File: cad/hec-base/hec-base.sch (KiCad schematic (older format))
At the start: 0 parts

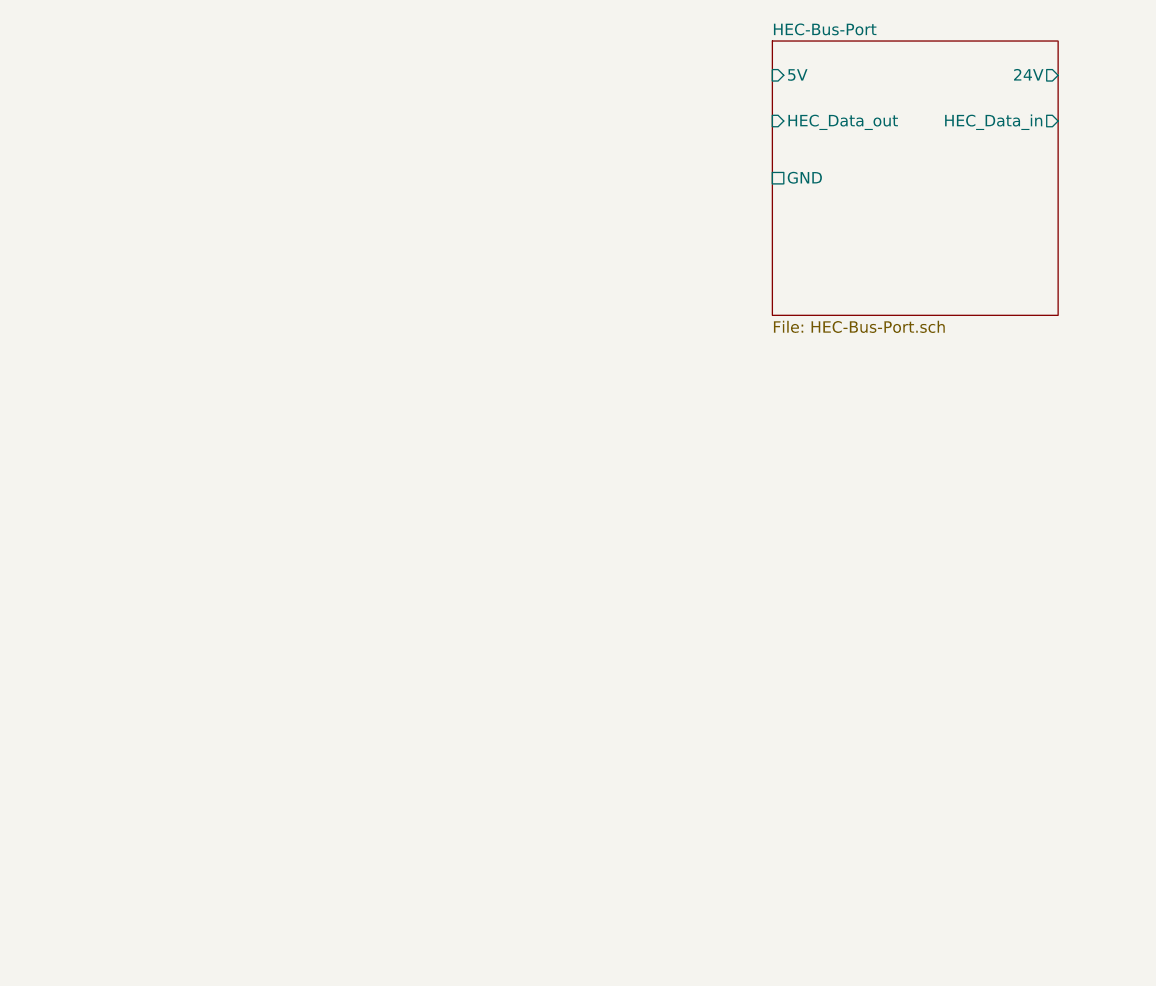
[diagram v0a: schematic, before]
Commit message: Power-Management schematics input and dimensioning done.
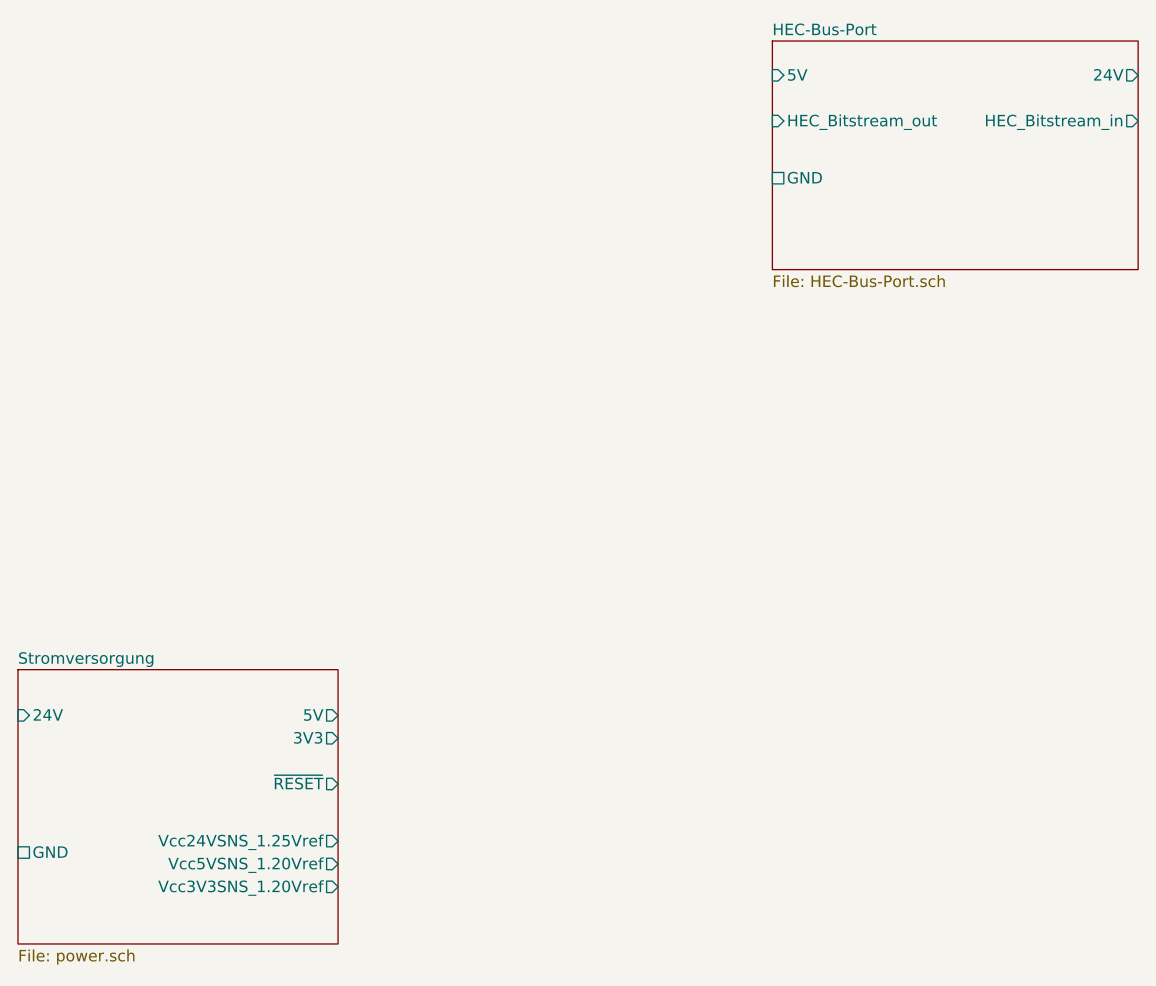
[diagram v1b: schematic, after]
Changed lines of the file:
@@
 $Descr A3 16535 11693
 encoding utf-8
-Sheet 1 2
+Sheet 1 3
 Title "Marienkäfer HEC-Basis-Bord"
 Date "2020-12-28"
@@
 $EndDescr
 $Sheet
-S 11850 1100 1250 1200
+S 8550 3850 1400 1200
+U 6012F6F5
+F0 "Stromversorgung" 50
+F1 "power.sch" 50
+F2 "24V" I L 8550 4050 50
+F3 "GND" U L 8550 4650 50
+F4 "5V" O R 9950 4050 50
+F5 "3V3" O R 9950 4150 50
+F6 "~RESET~" O R 9950 4350 50
+F7 "Vcc24VSNS_1.25Vref" O R 9950 4600 50
+F8 "Vcc5VSNS_1.20Vref" O R 9950 4700 50
+F9 "Vcc3V3SNS_1.20Vref" O R 9950 4800 50
+$EndSheet
+$Sheet
+S 11850 1100 1600 1000
 U 5FEA0914
 F0 "HEC-Bus-Port" 50
 F1 "HEC-Bus-Port.sch" 50
-F2 "HEC_Data_out" I L 11850 1450 50
-F3 "HEC_Data_in" O R 13100 1450 50
+F2 "HEC_Bitstream_out" I L 11850 1450 50
+F3 "HEC_Bitstream_in" O R 13450 1450 50
 F4 "5V" I L 11850 1250 50
-F5 "24V" O R 13100 1250 50
+F5 "24V" O R 13450 1250 50
 F6 "GND" U L 11850 1700 50
 $EndSheet

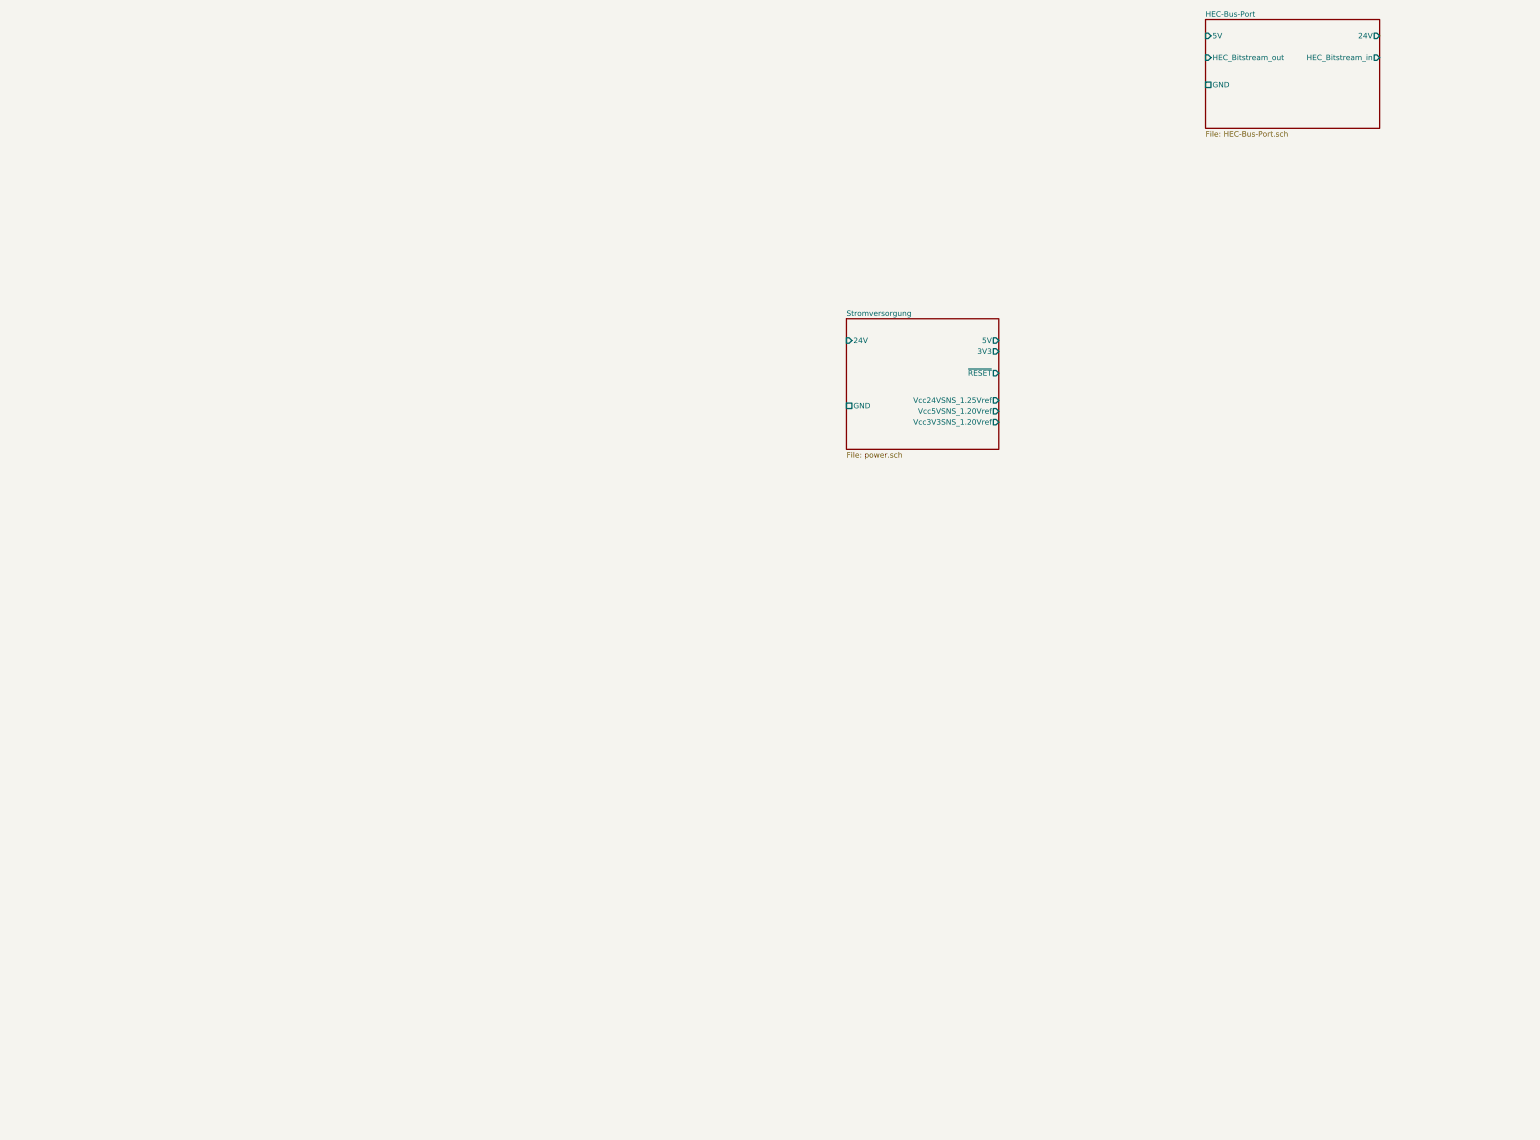
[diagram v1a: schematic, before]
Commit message: MCU-, Crypto- und One-Wire-Teil erstellt und dimensioniert, ERC bestanden, SLP geplottet, Footprints nur teilweise zugewiesen.
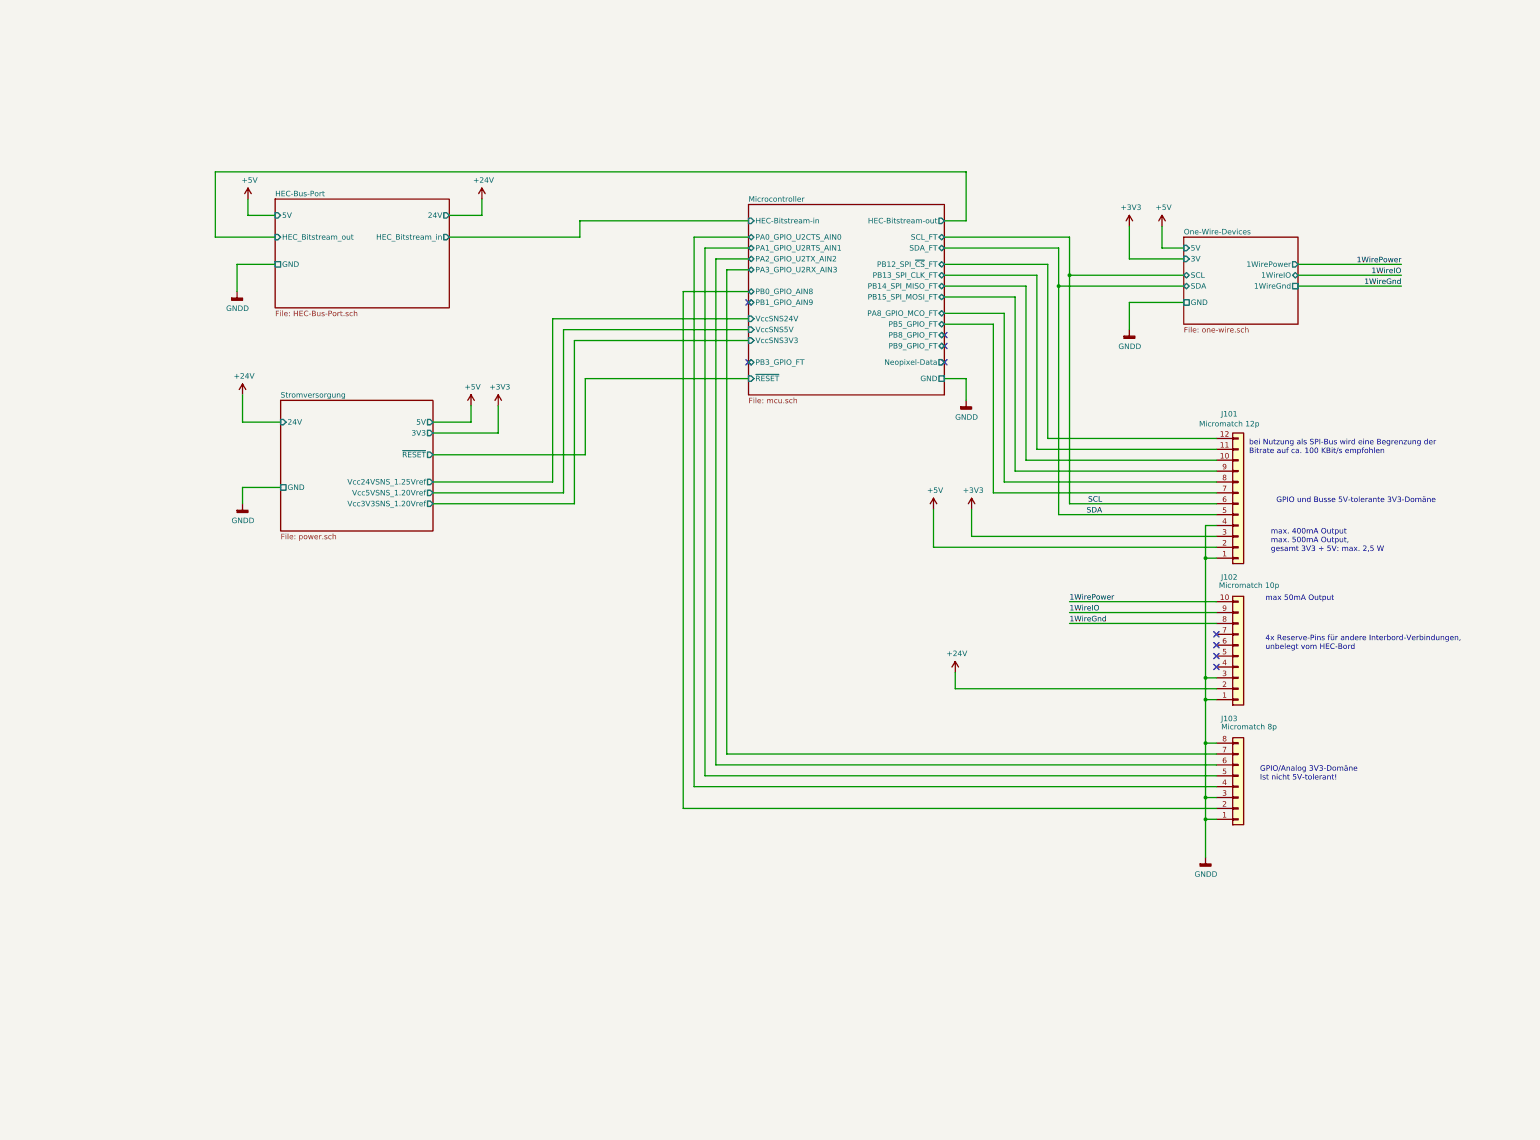
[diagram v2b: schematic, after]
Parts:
- added J101: Micromatch 12p, symbol Connector_Generic:Conn_01x12
- added J102: Micromatch 10p, Connectors_MicroMatch_MT:ConnectorMicromatch-10-SMD-polarized, symbol Connector_Generic:Conn_01x10
- added J103: Micromatch 8p, symbol Connector_Generic:Conn_01x08
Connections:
- new net +24V: J102.2 (Pin_2)
- new net +3V3: J101.3 (Pin_3)
- new net +5V: J101.2 (Pin_2)
- new net 1WireGnd: J102.8 (Pin_8)
- new net 1WireIO: J102.9 (Pin_9)
- new net 1WirePower: J102.10 (Pin_10)
- new net GNDD: J101.1 (Pin_1), J101.4 (Pin_4), J102.1 (Pin_1), J102.3 (Pin_3), J103.1 (Pin_1), J103.3 (Pin_3), J103.8 (Pin_8)
- new net Microcontroller/PA0_GPIO_U2CTS_AIN0: J103.4 (Pin_4)
- new net Microcontroller/PA1_GPIO_U2RTS_AIN1: J103.5 (Pin_5)
- new net Microcontroller/PA2_GPIO_U2TX_AIN2: J103.6 (Pin_6)
- new net Microcontroller/PA3_GPIO_U2RX_AIN3: J103.7 (Pin_7)
- new net Microcontroller/PA8_GPIO_MCO_FT: J101.8 (Pin_8)
- new net Microcontroller/PB0_GPIO_AIN8: J103.2 (Pin_2)
- new net Microcontroller/PB12_SPI_~CS~_FT: J101.12 (Pin_12)
- new net Microcontroller/PB13_SPI_CLK_FT: J101.11 (Pin_11)
- new net Microcontroller/PB14_SPI_MISO_FT: J101.10 (Pin_10)
- new net Microcontroller/PB15_SPI_MOSI_FT: J101.9 (Pin_9)
- new net Microcontroller/PB5_GPIO_FT: J101.7 (Pin_7)
- new net SCL: J101.6 (Pin_6)
- new net SDA: J101.5 (Pin_5)
- no-connect marks 0 -> 9
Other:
- note added: "4x Reserve-Pins für andere Interbord-Verbindungen,\nunbelegt vom HEC-Bord"
- note added: "GPIO und Busse 5V-tolerante 3V3-Domäne"
- note added: "GPIO/Analog 3V3-Domäne\nIst nicht 5V-tolerant!"
- note added: "bei Nutzung als SPI-Bus wird eine Begrenzung der \nBitrate auf ca. 100 KBit/s empfohlen"
- note added: "max 50mA Output"
- note added: "max. 400mA Output\nmax. 500mA Output, \ngesamt 3V3 + 5V: max. 2,5 W"

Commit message: MT-Marienkaefer: Footprints fertig zugewiesen.
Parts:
- J101: footprint (none) -> Connectors_MicroMatch_MT:ConnectorMicromatch-12-horizontal-THT
- J103: footprint (none) -> Connectors_MicroMatch_MT:ConnectorMicromatch-8-horizontal-THT
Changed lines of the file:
@@
 F 0 "J101" H 12068 4725 50  0000 C CNN
 F 1 "Micromatch 12p" H 12068 4816 50  0000 C CNN
-F 2 "" H 12150 5550 50  0001 C CNN
+F 2 "Connectors_MicroMatch_MT:ConnectorMicromatch-12-horizontal-THT" H 12150 5550 50  0001 C CNN
 F 3 "~" H 12150 5550 50  0001 C CNN
 	1    12150 5550
@@
 F 0 "J103" H 12068 7525 50  0000 C CNN
 F 1 "Micromatch 8p" H 12250 7600 50  0000 C CNN
-F 2 "" H 12150 8150 50  0001 C CNN
+F 2 "Connectors_MicroMatch_MT:ConnectorMicromatch-8-horizontal-THT" H 12150 8150 50  0001 C CNN
 F 3 "~" H 12150 8150 50  0001 C CNN
 	1    12150 8150
